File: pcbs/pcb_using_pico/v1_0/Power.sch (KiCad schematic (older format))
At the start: 28 parts, among them J3 Barrel_Jack, U5 BQ24072RGT, U6 AMS1117-3.3, U7 AMS1117-5.0

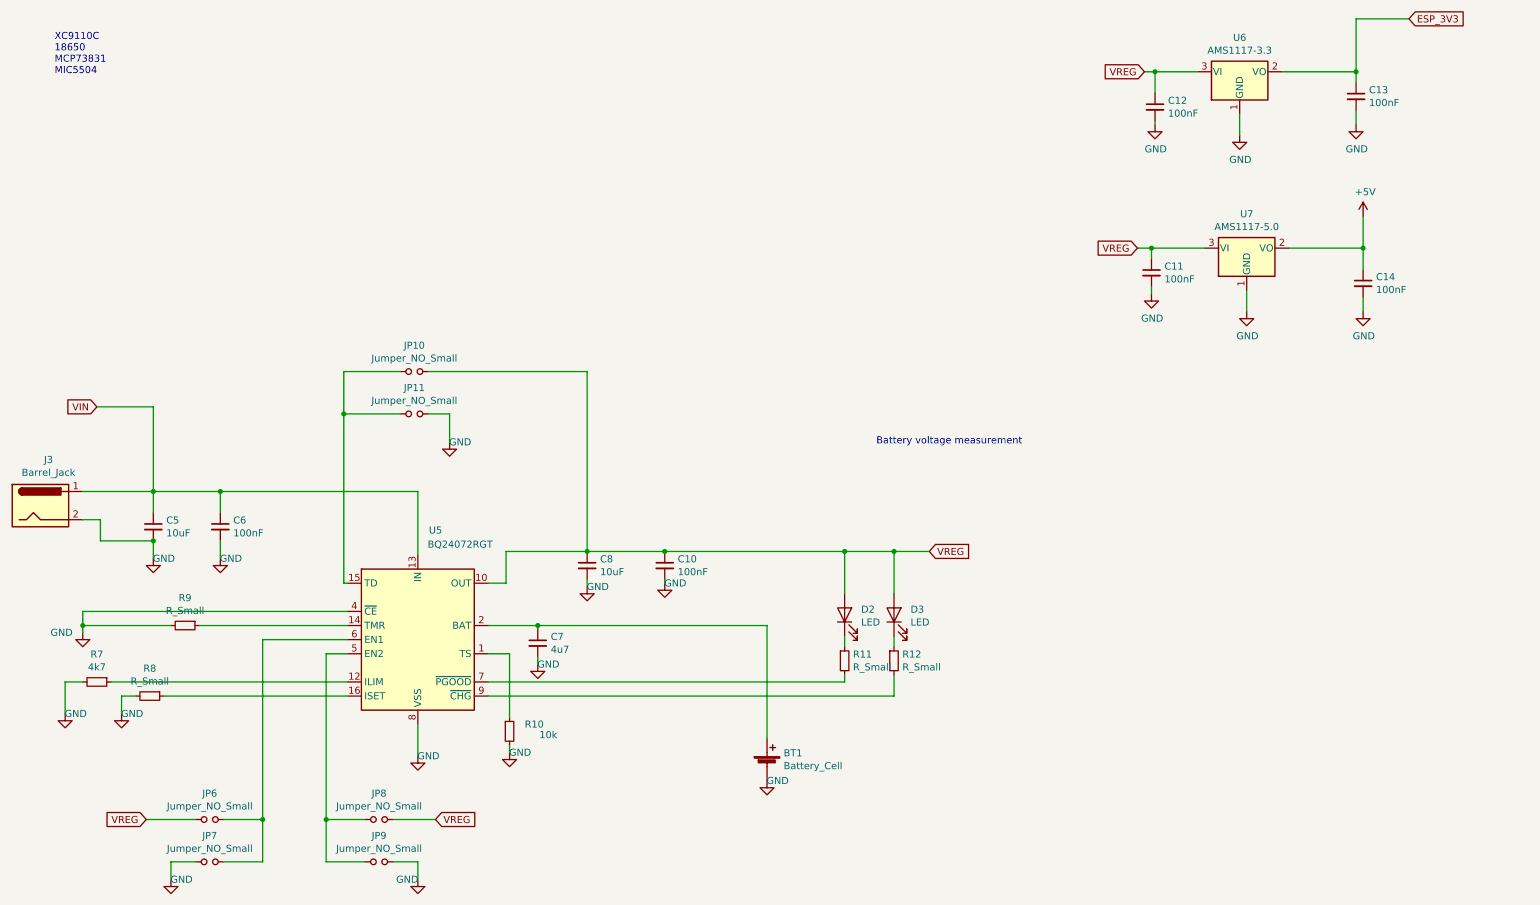
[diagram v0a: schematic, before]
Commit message: V2.0 PCB, new charger IC, USB power option
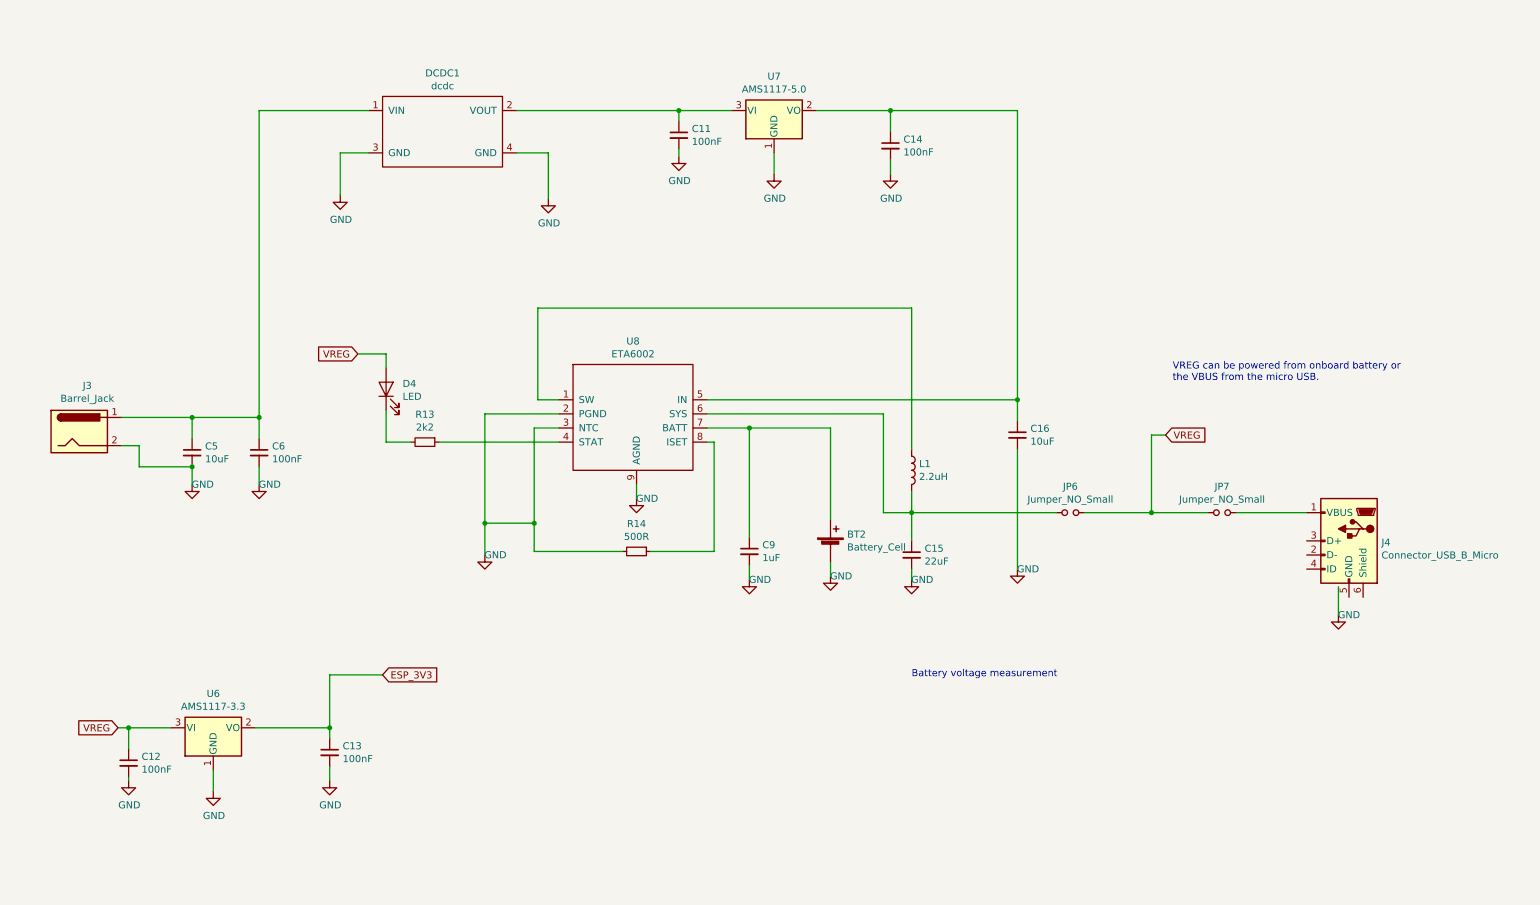
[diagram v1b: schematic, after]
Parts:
- removed BT1: Battery_Cell, Battery:BatteryHolder_Keystone_1042_1x18650, symbol Device:Battery_Cell
- removed C10: 100nF, Capacitor_SMD:C_0805_2012Metric, symbol Device:C_Small
- removed C7: 4u7, Capacitor_SMD:C_1206_3216Metric_Pad1.42x1.75mm_HandSolder, symbol Device:C_Small
- removed C8: 10uF, Capacitor_SMD:C_1206_3216Metric_Pad1.42x1.75mm_HandSolder, symbol Device:C_Small
- removed D2, D3: LED, LED_SMD:LED_0805_2012Metric_Pad1.15x1.40mm_HandSolder, symbol Device:LED
- removed JP10, JP11, JP8, JP9: Jumper_NO_Small, Jumper:SolderJumper-2_P1.3mm_Open_RoundedPad1.0x1.5mm, symbol Device:Jumper_NO_Small
- removed R10: 10k, Resistor_SMD:R_0805_2012Metric, symbol Device:R_Small
- removed R11, R12, R8, R9: R_Small, Resistor_SMD:R_0805_2012Metric, symbol Device:R_Small
- removed R7: 4k7, Resistor_SMD:R_0805_2012Metric, symbol Device:R_Small
- removed U5: BQ24072RGT, Package_DFN_QFN:VQFN-16-1EP_3x3mm_P0.5mm_EP1.6x1.6mm, symbol Battery_Management:BQ24072RGT
- added BT2: Battery_Cell, Battery:BatteryHolder_Keystone_1042_1x18650, symbol Device:Battery_Cell
- added C15: 22uF, Capacitor_SMD:C_1206_3216Metric_Pad1.42x1.75mm_HandSolder, symbol Device:C_Small
- added C16: 10uF, Capacitor_SMD:C_1206_3216Metric_Pad1.42x1.75mm_HandSolder, symbol Device:C_Small
- added C9: 1uF, Capacitor_SMD:C_1206_3216Metric_Pad1.42x1.75mm_HandSolder, symbol Device:C_Small
- added D4: LED, LED_SMD:LED_0805_2012Metric_Pad1.15x1.40mm_HandSolder, symbol Device:LED
- added DCDC1: dcdc, Connector_PinHeader_2.54mm:PinHeader_1x04_P2.54mm_Vertical, symbol New_Library:dcdc
- added J4: Connector_USB_B_Micro, Connector_USB:USB_Micro-B_GCT_USB3076-30-A, symbol cq1re1-cache:Connector_USB_B_Micro
- added L1: 2.2uH, Inductor_SMD:L_Coilcraft_LPS5030, symbol Device:L
- added R13: 2k2, Resistor_SMD:R_0805_2012Metric, symbol Device:R_Small
- added R14: 500R, Resistor_SMD:R_0805_2012Metric, symbol Device:R_Small
- added U8: ETA6002, Package_SO:SOIC-8-1EP_3.9x4.9mm_P1.27mm_EP2.514x3.2mm, symbol pak_breakout:ETA6002
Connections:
- net GND: now also BT2.2 (-), C15.2, C16.2, C9.2, DCDC1.3 (GND), DCDC1.4 (GND), R14.2, U8.2 (PGND), U8.3 (NTC), U8.9 (AGND); no longer JP7.1
- net VREG: now also JP7.1, D4.2 (A); no longer C11.1, U7.3 (VI)
- net at JP6.2: now also C15.1, L1.2, U8.6 (SYS); no longer JP7.2
- net +5V: no longer names the net of C14.1, U7.2 (VO)
- net +5V: now also C16.1, U8.5 (IN)
- net VIN: no longer names the net of C5.1, C6.1, J3.1
- net VIN: now also DCDC1.1 (VIN)
- new net: C11.1, DCDC1.2 (VOUT), U7.3 (VI)
- new net: L1.1, U8.1 (SW)
- new net: R13.1, U8.4 (STAT)
- new net: BT2.1 (+), C9.1, U8.7 (BATT)
- new net: R14.1, U8.8 (ISET)
- new net: D4.1 (K), R13.2
- new net: J4.1 (VBUS), JP7.2
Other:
- note added: "VREG can be powered from onboard battery or\nthe VBUS from the micro USB."
- note removed: "XC9110C\n18650\nMCP73831\nMIC5504\n"
- moved on the sheet: C11, C12, C13, C14, C5, C6, J3, U6, U7
